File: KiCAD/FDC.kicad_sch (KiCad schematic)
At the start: 24 parts, among them J2 Conn_02x20_Odd_Even, J3 SD_Card, Q1 SSM3K324RLFCT-ND, Q2 SSM3K324RLFCT-ND, U1 SN74LVCC4245ADWR, U2 Pico, U3 SN74LVCC4245ADWR, U4 SN74LVCC4245ADWR, U5 SN74LVCC4245ADWR

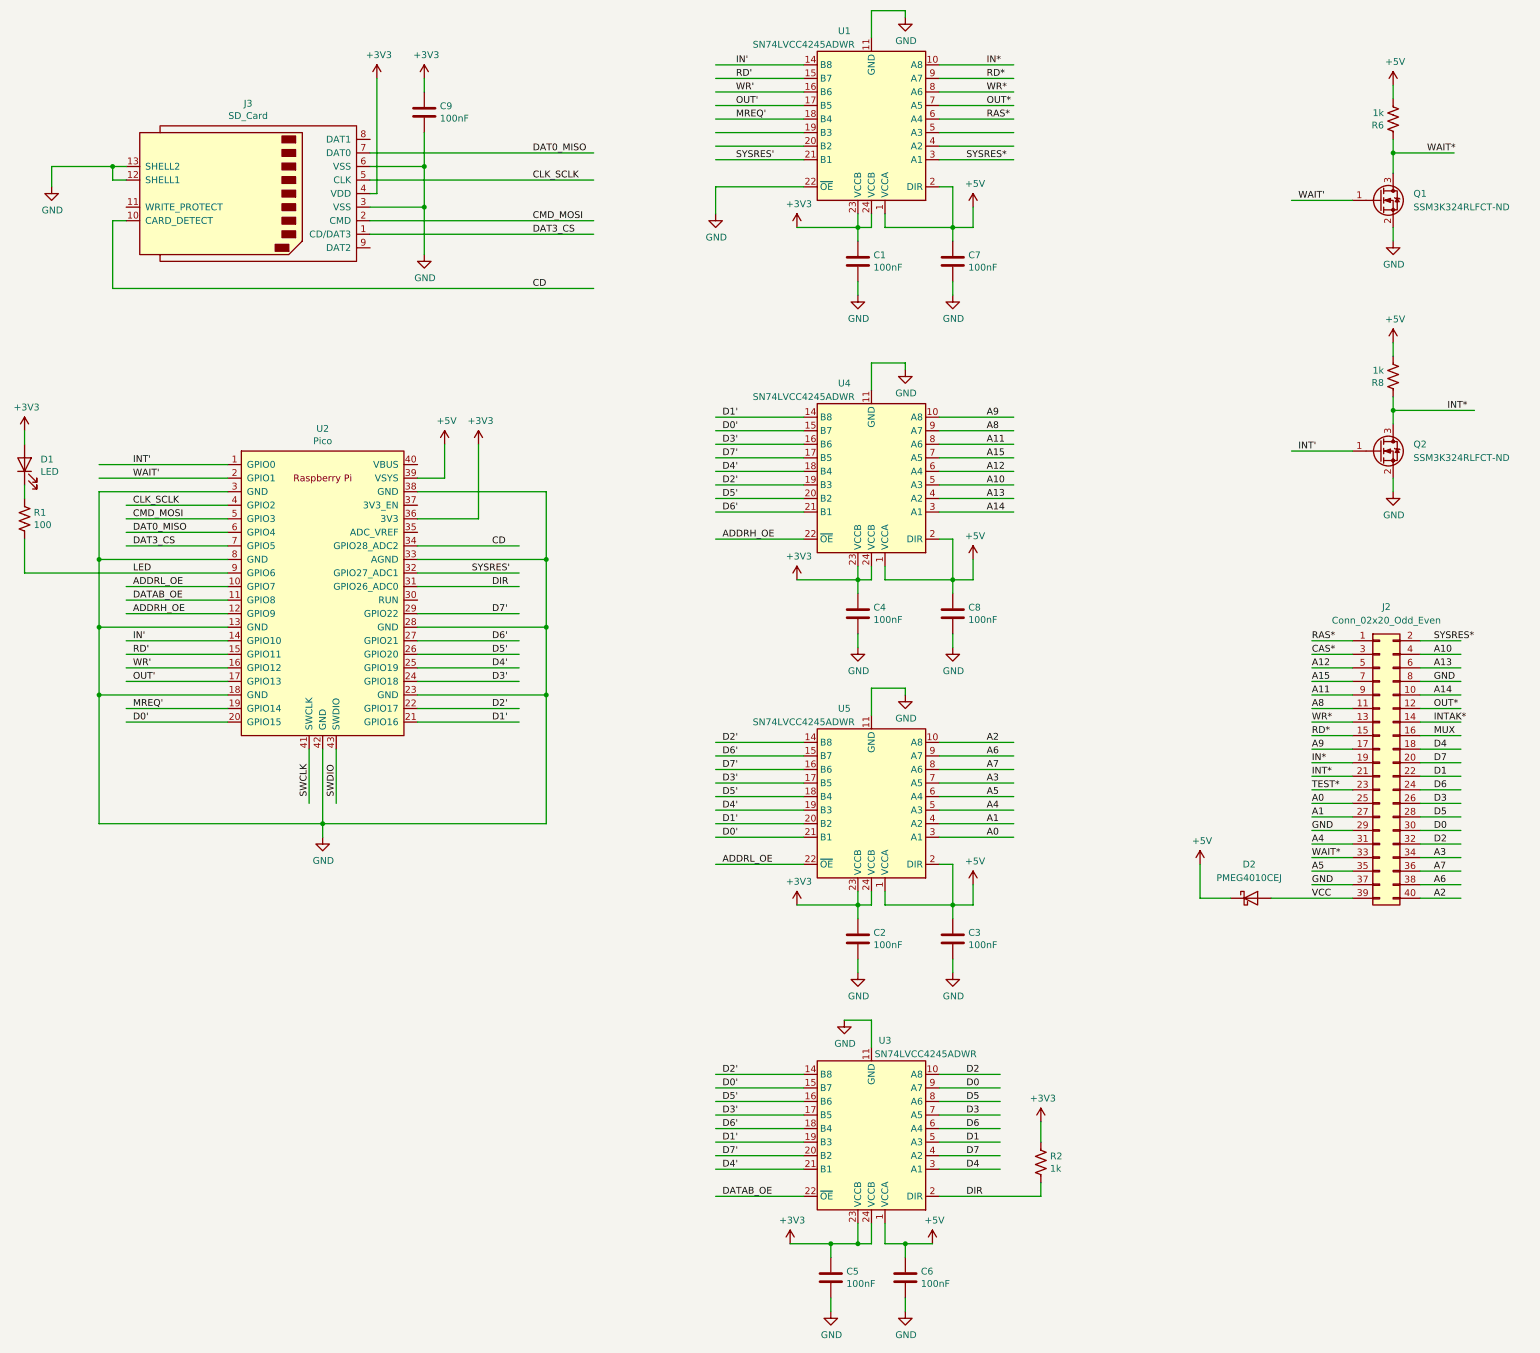
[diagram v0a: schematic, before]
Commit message: Updates schematic part numbers
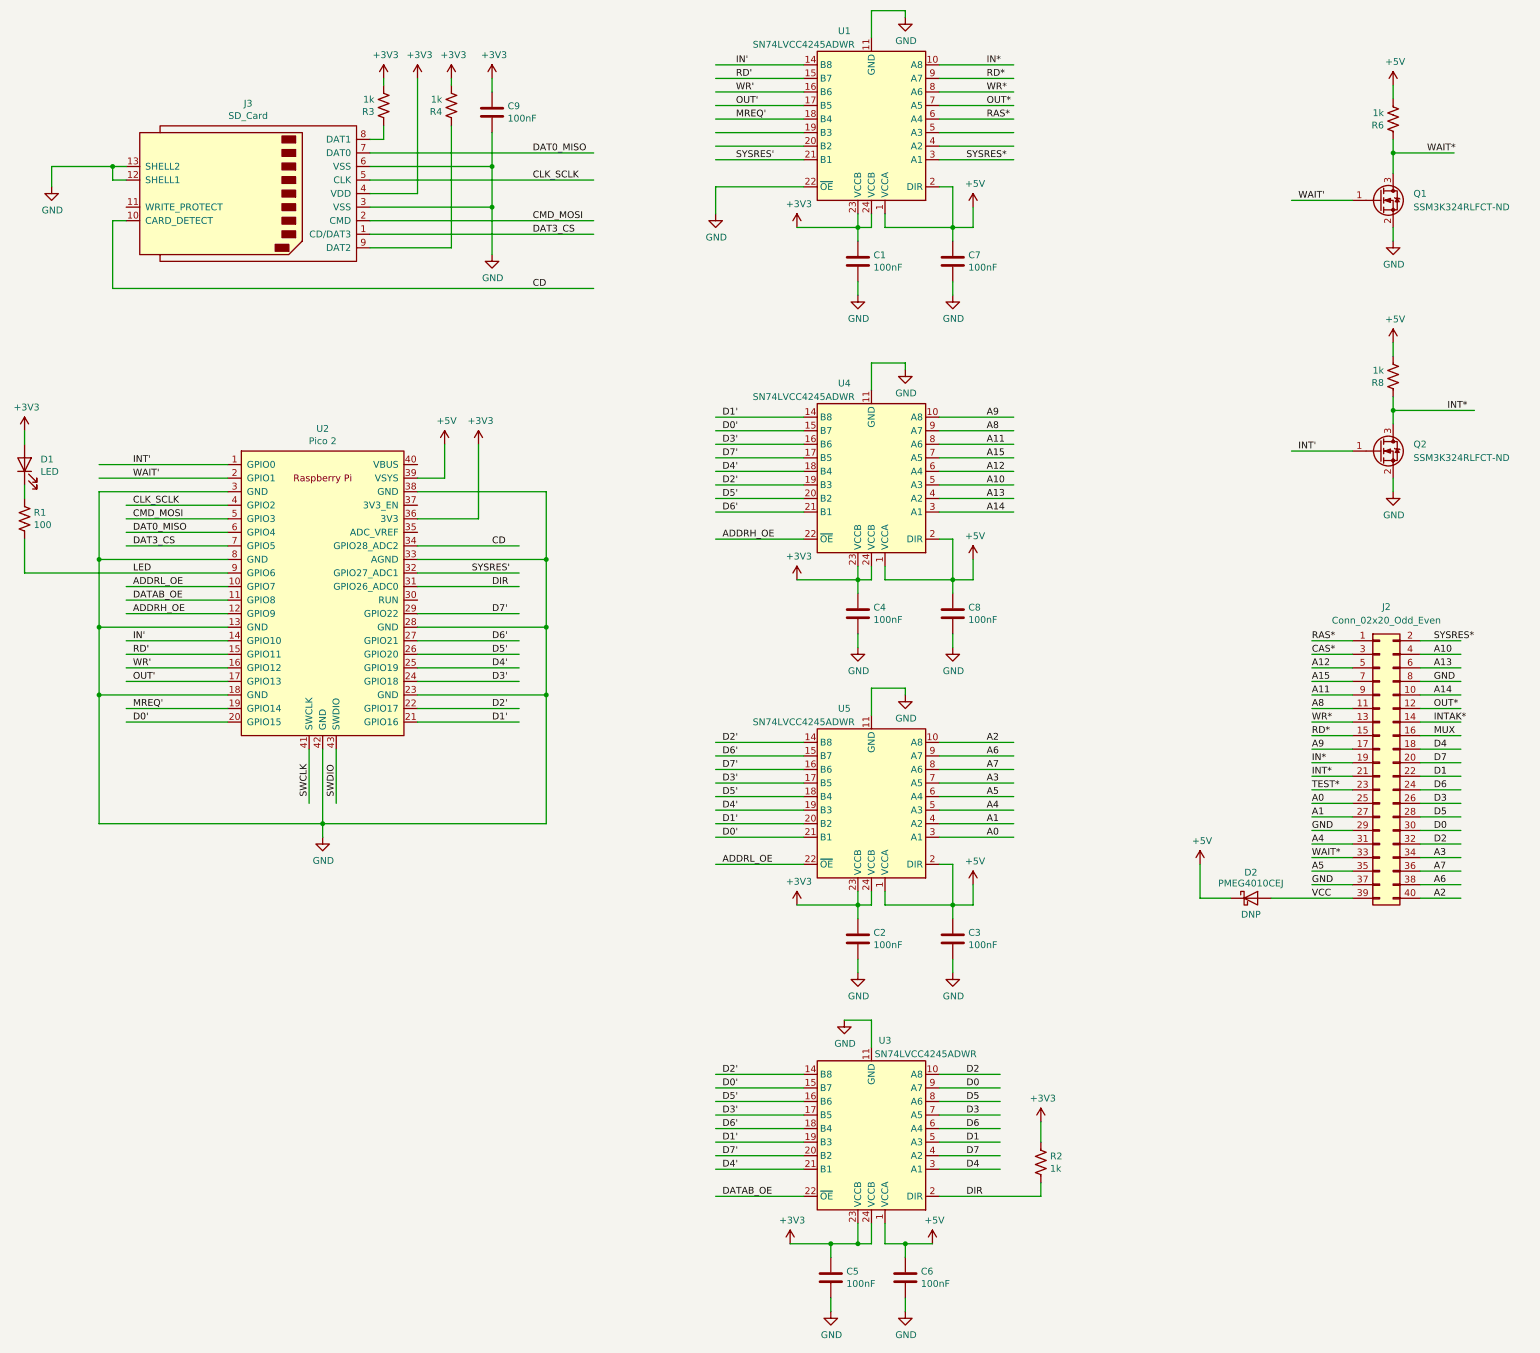
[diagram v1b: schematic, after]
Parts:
- added R3, R4: 1k, Resistor_SMD:R_0805_2012Metric_Pad1.20x1.40mm_HandSolder, symbol Device:R_US
- D2: Place (none) -> DNP
- U2: value Pico -> Pico 2; Cost 4.00 -> 5.00; Digikey 2648-SC0915CT-ND -> 2648-SC1631CT-ND
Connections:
- net +3V3: now also R3.2, R4.2
- net at J3.8 (DAT1): now also R3.1
- net at J3.9 (DAT2): now also R4.1
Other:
- moved on the sheet: C9
